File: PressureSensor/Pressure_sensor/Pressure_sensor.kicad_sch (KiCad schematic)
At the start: 78 parts, among them J1 Power Input, J2 Conn_01x04_Pin, J3 Screw_Terminal_01x03, J4 Conn_02x03_Odd_Even, J5 Valve Terminal, J6 Conn_01x05_Pin, J7 USB_A, K1 SANYOU_SRD_Form_C, Q1 BC848, SW1 SW_SPST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

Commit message: push
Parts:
- removed U4: EA_T123X-I2C, Display:Adafruit_SSD1306_No_Mounting_Holes, symbol Display_Character:EA_T123X-I2C
- added U5: DM-OLED096-636, DM-OLED096-636:MODULE_DM-OLED096-636, symbol DM-OLED096-636:DM-OLED096-636
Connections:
- net +5V: now also U5.2 (VCC_IN)
- net GND: now also U5.1 (GND)
- net SCL: now also U5.3 (SCL)
- net SDA: now also U5.4 (SDA)
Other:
- note removed: "Scratch"

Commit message: Push
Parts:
- D8: footprint Diode_SMD:D_SOD-523 -> Diode_SMD:D_SOD-123
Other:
- moved on the sheet: BT1, BT2, BT3, J1, R1, R2, SW6

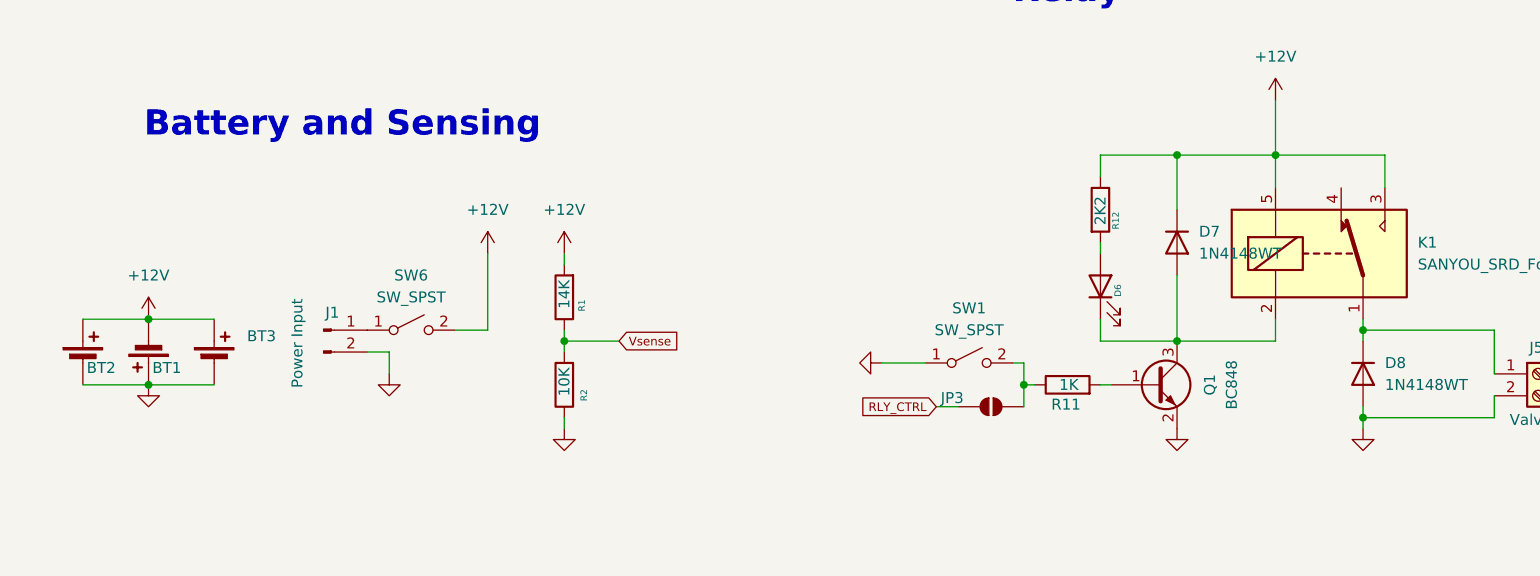
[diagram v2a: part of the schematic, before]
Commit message: push
1. Battery 2p1a to 3S
2. Relay Switch - pull down to pull up
3. Scratch - Inserted true OLED display
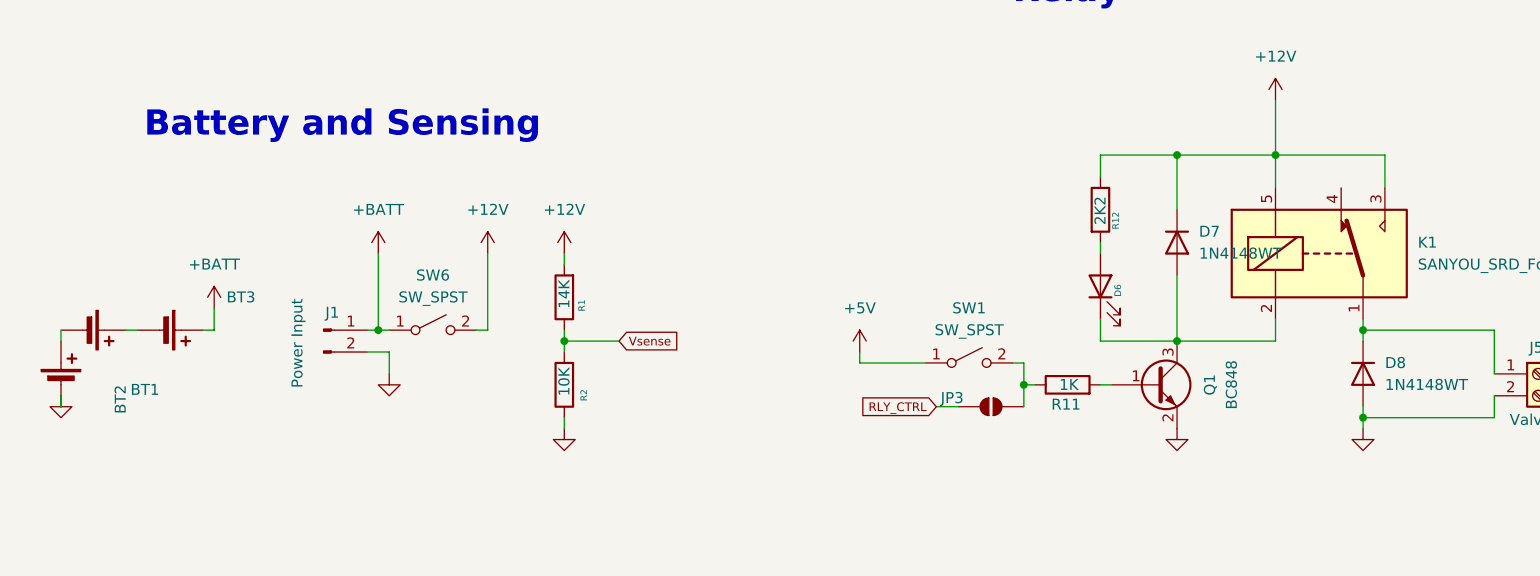
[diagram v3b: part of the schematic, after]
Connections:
- net +12V: no longer BT1.1 (+), BT2.2 (-), BT3.1 (+)
- net +5V: now also SW1.1 (A)
- net GND: no longer BT2.1 (+), BT3.2 (-), SW1.1 (A)
- net +BATT: now reaches J1.1 (Pin_1), SW6.1 (A)
- net +BATT: now also BT3.1 (+)
- new net: BT1.1 (+), BT2.2 (-)
- new net: BT2.1 (+), BT3.2 (-)
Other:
- moved on the sheet: BT1, BT2, BT3, SW6

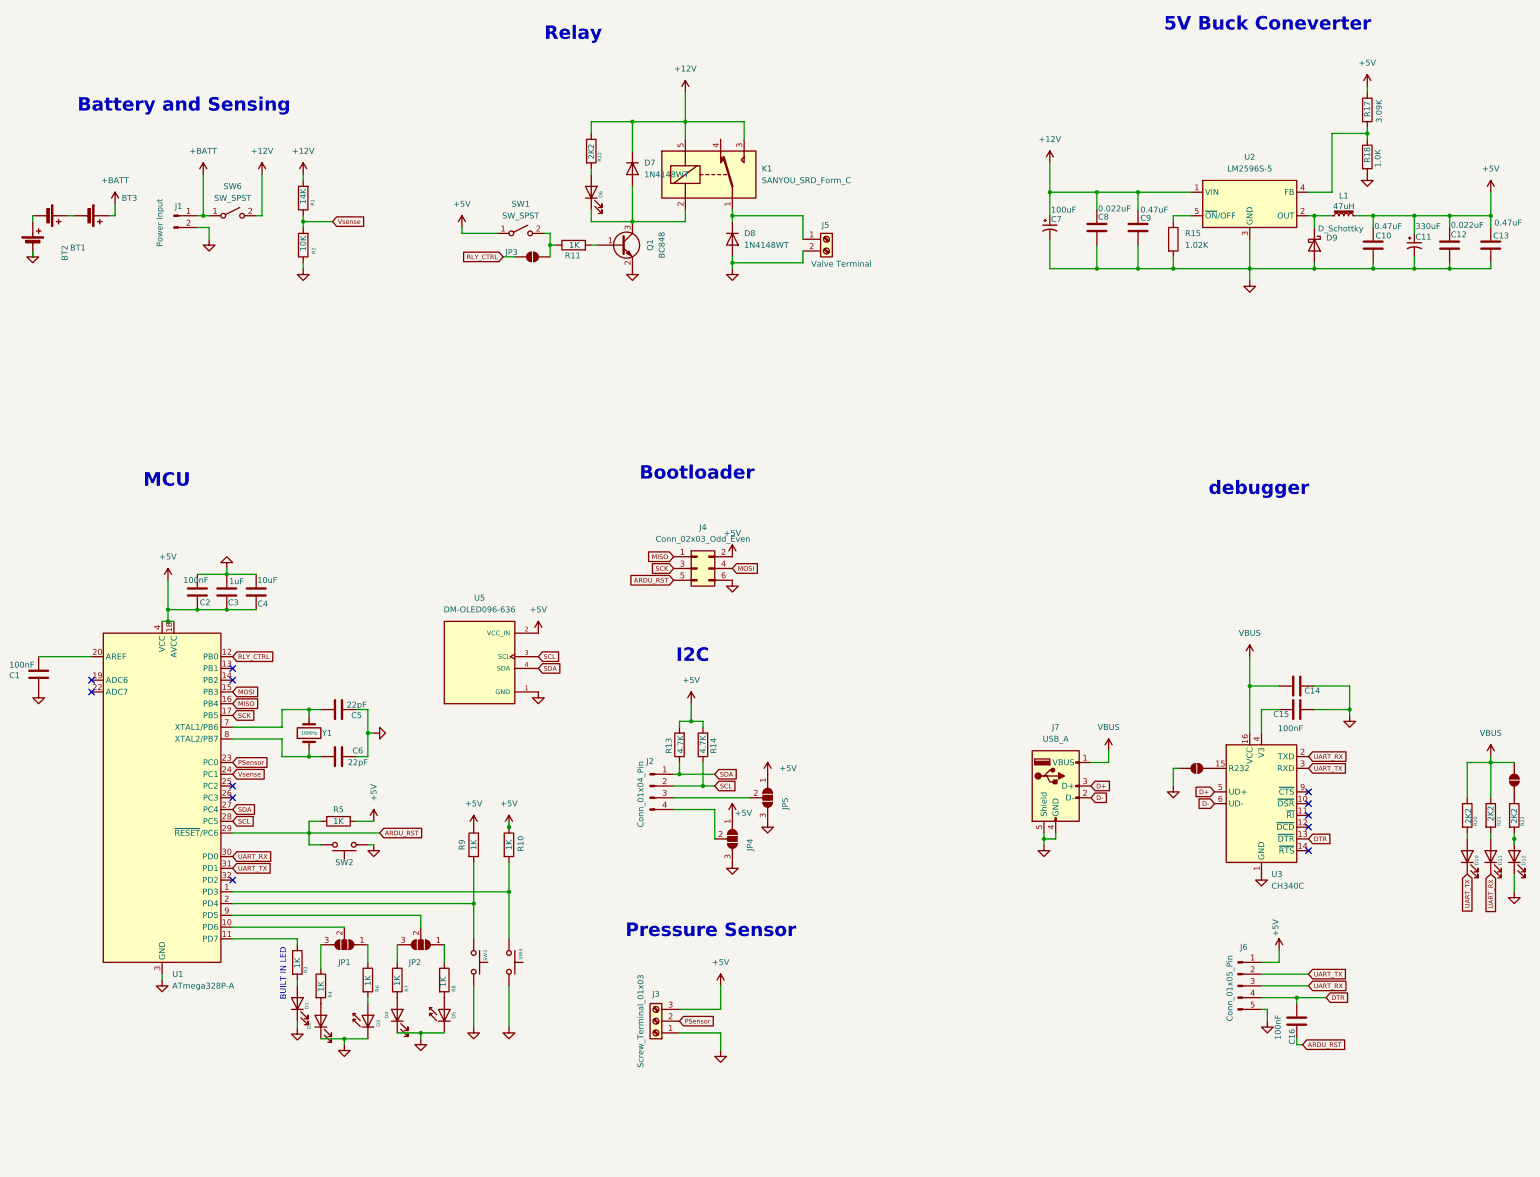
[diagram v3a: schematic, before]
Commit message: For Checking
- Data tracks
- Components placement

do not mind the ff will do after this checking:
- power tracks - zoning
- zone layer
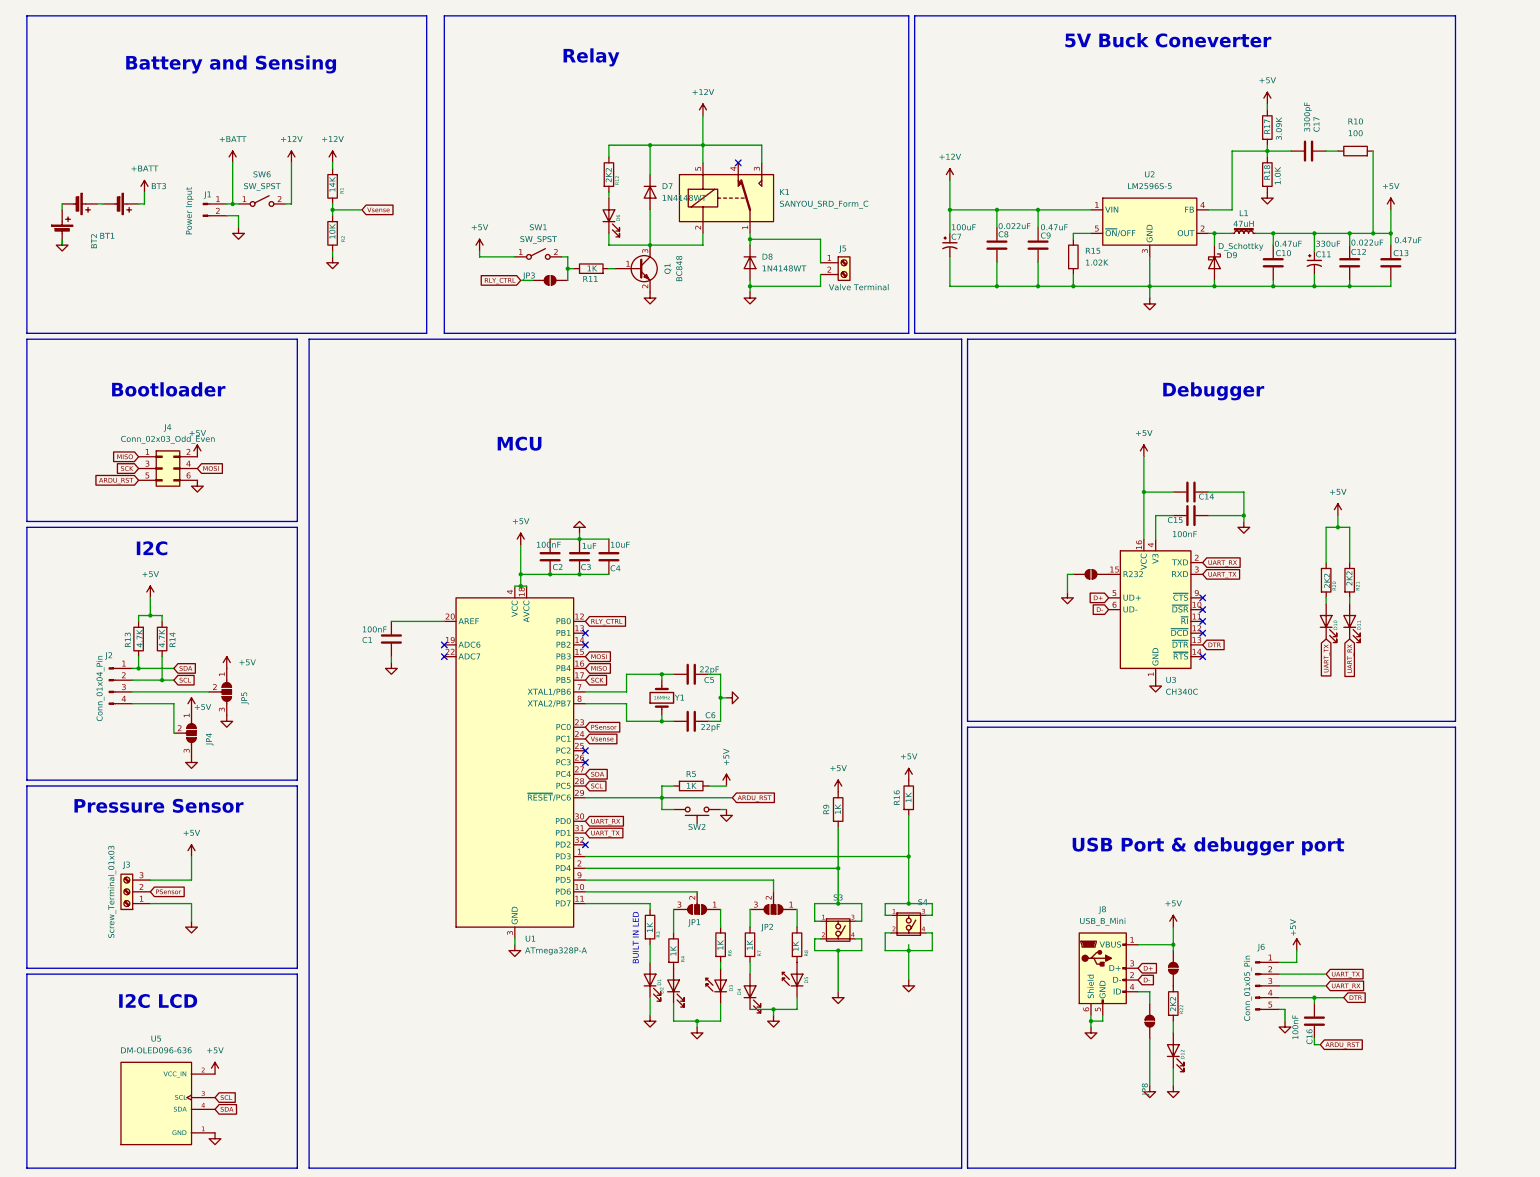
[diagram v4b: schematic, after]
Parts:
- removed J7: USB_A, Connector_USB:USB_A_Connfly_DS1095, symbol Connector:USB_A
- removed SW3, SW4: SW_Push, Button_Switch_THT:SW_PUSH_6mm_H9.5mm, symbol Switch:SW_Push
- added C17: 3300pF, Capacitor_SMD:C_0603_1608Metric, symbol Device:C
- added J8: USB_B_Mini, Connector_USB:USB_Mini-B_Lumberg_2486_01_Horizontal, symbol Connector:USB_B_Mini
- added JP8: SolderJumper_2_Open, Jumper:SolderJumper-2_P1.3mm_Open_RoundedPad1.0x1.5mm, symbol Jumper:SolderJumper_2_Open
- added R16: 1K, Resistor_SMD:R_0603_1608Metric, symbol Device:R
- added S3, S4: TS04-66-70-BK-160-SMT, TS04-66-70-BK-160-SMT:SW_TS04-66-70-BK-160-SMT, symbol TS04-66-70-BK-160-SMT:TS04-66-70-BK-160-SMT
- J3: footprint Connector_PinSocket_2.54mm:PinSocket_1x03_P2.54mm_Vertical -> TerminalBlock:TerminalBlock_MaiXu_MX126-5.0-03P_1x03_P5.00mm
- J5: footprint Connector_PinSocket_2.54mm:PinSocket_1x02_P2.54mm_Vertical -> TerminalBlock:TerminalBlock_MaiXu_MX126-5.0-02P_1x02_P5.00mm
- JP1, JP2, JP4, JP5: footprint Jumper:SolderJumper-3_P1.3mm_Open_Pad1.0x1.5mm -> Jumper:SolderJumper-3_P1.3mm_Open_RoundedPad1.0x1.5mm
- JP6, JP7: footprint Jumper:SolderJumper-2_P1.3mm_Open_Pad1.0x1.5mm -> Jumper:SolderJumper-2_P1.3mm_Open_RoundedPad1.0x1.5mm
- R10: value 1K -> 100; LCSC C21190 -> (none); Order  Status Ordered -> (none); Order Link https://shopee.ph/100pcs-0603-SMD-1-8W-chip-resistor-resist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 -> (none)
- SW2: footprint Button_Switch_THT:SW_PUSH_6mm_H9.5mm -> Button_Switch_SMD:SW_SPST_FSMSM
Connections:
- net VBUS is gone; now on net +5V: C14.1, JP7.2 (B), R20.1, R21.1, U3.16 (VCC)
- net +5V: now also R10.2, J8.1 (VBUS), R16.1; no longer R10.1
- net D+: now also J8.3 (D+)
- net D-: now also J8.2 (D-)
- net GND: now also J8.5 (GND), J8.6 (Shield), JP8.2 (B), S3.2, S3.4, S4.2, S4.4
- net at U1.1 (PD3): now also R16.2, S4.1, S4.3; no longer R10.2
- net at R9.2, U1.2 (PD4): now also S3.1, S3.3
- net at R17.2, R18.1, U2.4 (FB): now also C17.1
- new net: C17.2, R10.1
- new net: J8.4 (ID), JP8.1 (A)
- no-connect marks 12 -> 13
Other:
- note added: "Debugger"
- note added: "I2C LCD"
- note added: "USB Port & debugger port"
- note removed: "debugger"
- moved on the sheet: BT1, BT2, BT3, C1, C10, C11, C12, C13, C14, C15, C16, C2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
